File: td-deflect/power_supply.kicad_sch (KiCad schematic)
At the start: 18 parts, among them J1 Conn_01x08_Socket, J1 Conn_01x12_Socket, J18 Conn_01x02_Male, J2 Conn_01x02_Male, J3 Conn_01x04_Male

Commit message: fix drc errors
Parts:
- J18, J2: symbol Connector:Conn_01x02_Male -> Connector:Conn_01x02_Pin
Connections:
- net +3.3V: no longer J1.1 (Pin_1), J1.2 (Pin_2), J3.1 (Pin_1), JP2.2 (B), R30.1
- new net B+C: J1.1 (Pin_1), J1.2 (Pin_2), J3.1 (Pin_1), JP2.2 (B), R30.1

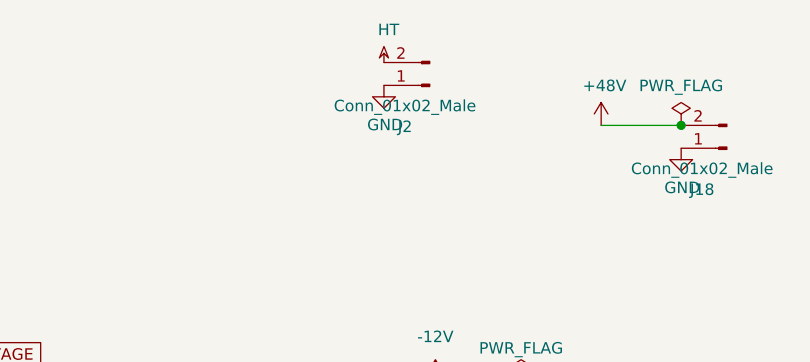
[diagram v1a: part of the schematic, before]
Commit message: fix remaining erc errors
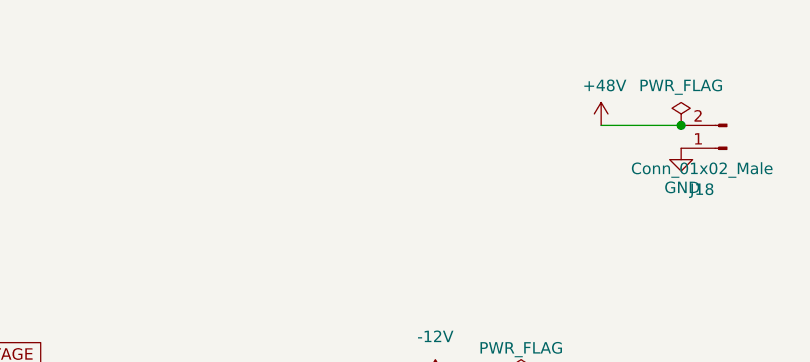
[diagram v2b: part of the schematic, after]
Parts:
- removed J2: Conn_01x02_Male, Connector_Phoenix_MSTB:PhoenixContact_MSTBVA_2,5_2-G_1x02_P5.00mm_Vertical, symbol Connector:Conn_01x02_Pin
- J3: symbol Connector:Conn_01x04_Male -> Connector:Conn_01x04_Pin
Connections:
- net +3.3V renamed B+F
- net B+F: no longer J1.1 (Pin_1), J1.2 (Pin_2), JP1.1 (A), R73.1
- new net B+H: J1.1 (Pin_1), J1.2 (Pin_2), JP1.1 (A), R73.1
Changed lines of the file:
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@@
-    )
-  )
-  (symbol (lib_id "Connector:Conn_01x02_Pin") (at 170.18 24.13 180) (unit 1)
-    (in_bom yes) (on_board yes) (dnp no)
-    (property "Reference" "J2" (at 167.4368 28.7274 0)
-      (effects (font (size 1.27 1.27)))
-    )
-    (property "Value" "Conn_01x02_Male" (at 167.4368 26.416 0)
-      (effects (font (size 1.27 1.27)))
-    )
-    (property "Footprint" "Connector_Phoenix_MSTB:PhoenixContact_MSTBVA_2,5_2-G_1x02_P5.00mm_Vertical" (at 170.18 24.13 0)
-      (effects (font (size 1.27 1.27)) hide)
-    )
-    (property "Datasheet" "~" (at 170.18 24.13 0)
-      (effects (font (size 1.27 1.27)) hide)
-    )
-    (property "Digikey" "277-1150-ND " (at 170.18 24.13 0)
-      (effects (font (size 1.27 1.27)) hide)
-    )
-    (pin "1")
-    (pin "2")
-    (instances
-      (project "td-deflect"
-        (path "/55a1a5e1-4d11-4c3e-b2b4-b9d50ddc5f9d/00000000-0000-0000-0000-00005d9d9196"
-          (reference "J2") (unit 1)
-        )
-      )
-    )
-  )
-  (symbol (lib_id "power:HT") (at 165.1 21.59 0) (unit 1)
-    (in_bom yes) (on_board yes) (dnp no)
-    (property "Reference" "#PWR0101" (at 165.1 18.542 0)
-      (effects (font (size 1.27 1.27)) hide)
-    )
-    (property "Value" "HT" (at 165.608 17.9578 0)
-      (effects (font (size 1.27 1.27)))
-    )
-    (property "Footprint" "" (at 165.1 21.59 0)
-      (effects (font (size 1.27 1.27)) hide)
-    )
-    (property "Datasheet" "" (at 165.1 21.59 0)
-      (effects (font (size 1.27 1.27)) hide)
-    )
-    (pin "1")
-    (instances
-      (project "td-deflect"
-        (path "/55a1a5e1-4d11-4c3e-b2b4-b9d50ddc5f9d/00000000-0000-0000-0000-00005d9d9196"
-          (reference "#PWR0101") (unit 1)
-        )
-      )
-    )
-  )
-  (symbol (lib_id "power:GND") (at 165.1 24.13 0) (unit 1)
-    (in_bom yes) (on_board yes) (dnp no)
-    (property "Reference" "#PWR0102" (at 165.1 30.48 0)
-      (effects (font (size 1.27 1.27)) hide)
-    )
-    (property "Value" "GND" (at 165.227 28.5242 0)
-      (effects (font (size 1.27 1.27)))
-    )
-    (property "Footprint" "" (at 165.1 24.13 0)
-      (effects (font (size 1.27 1.27)) hide)
-    )
-    (property "Datasheet" "" (at 165.1 24.13 0)
-      (effects (font (size 1.27 1.27)) hide)
-    )
-    (pin "1")
-    (instances
-      (project "td-deflect"
-        (path "/55a1a5e1-4d11-4c3e-b2b4-b9d50ddc5f9d/00000000-0000-0000-0000-00005d9d9196"
-          (reference "#PWR0102") (unit 1)
-        )
-      )
     )
   )
@@
     )
   )
-  (symbol (lib_name "PWR_FLAG_1") (lib_id "power:PWR_FLAG") (at 38.1 43.18 0) (unit 1)
+  (symbol (lib_id "power:PWR_FLAG") (at 38.1 43.18 0) (unit 1)
     (in_bom yes) (on_board yes) (dnp no) (fields_autoplaced)
     (property "Reference" "#FLG02" (at 38.1 41.275 0)
@@
     )
   )
-  (symbol (lib_name "PWR_FLAG_1") (lib_id "power:PWR_FLAG") (at 104.14 43.18 0) (unit 1)
+  (symbol (lib_id "power:PWR_FLAG") (at 104.14 43.18 0) (unit 1)
     (in_bom yes) (on_board yes) (dnp no) (fields_autoplaced)
     (property "Reference" "#FLG04" (at 104.14 41.275 0)
@@
     )
   )
-  (symbol (lib_id "Connector:Conn_01x04_Male") (at 259.08 101.6 0) (mirror y) (unit 1)
+  (symbol (lib_id "Connector:Conn_01x04_Pin") (at 259.08 101.6 0) (mirror y) (unit 1)
     (in_bom yes) (on_board yes) (dnp no) (fields_autoplaced)
     (property "Reference" "J3" (at 260.35 101.5999 0)
@@
     )
   )
-  (symbol (lib_name "PWR_FLAG_2") (lib_id "power:PWR_FLAG") (at 173.99 67.31 180) (unit 1)
+  (symbol (lib_id "power:PWR_FLAG") (at 173.99 67.31 180) (unit 1)
     (in_bom yes) (on_board yes) (dnp no) (fields_autoplaced)
     (property "Reference" "#FLG05" (at 173.99 69.215 0)
@@
     )
   )
-  (symbol (lib_name "PWR_FLAG_2") (lib_id "power:PWR_FLAG") (at 180.34 57.15 0) (unit 1)
+  (symbol (lib_id "power:PWR_FLAG") (at 180.34 57.15 0) (unit 1)
     (in_bom yes) (on_board yes) (dnp no) (fields_autoplaced)
     (property "Reference" "#FLG06" (at 180.34 55.245 0)
@@
     )
   )
-  (symbol (lib_name "PWR_FLAG_3") (lib_id "power:PWR_FLAG") (at 212.09 68.58 180) (unit 1)
+  (symbol (lib_id "power:PWR_FLAG") (at 212.09 68.58 180) (unit 1)
     (in_bom yes) (on_board yes) (dnp no) (fields_autoplaced)
     (property "Reference" "#FLG07" (at 212.09 70.485 0)
@@
     )
   )
-  (symbol (lib_name "PWR_FLAG_1") (lib_id "power:PWR_FLAG") (at 71.12 43.18 0) (unit 1)
+  (symbol (lib_id "power:PWR_FLAG") (at 71.12 43.18 0) (unit 1)
     (in_bom yes) (on_board yes) (dnp no) (fields_autoplaced)
     (property "Reference" "#FLG03" (at 71.12 41.275 0)

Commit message: usb
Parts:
- added J17: Barrel_Jack, Connector_BarrelJack:BarrelJack_CLIFF_FC681465S_SMT_Horizontal, symbol Connector:Barrel_Jack_Switch
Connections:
- net +48V: now also J17.1
- net GND: now also J17.2
- no-connect marks 6 -> 7
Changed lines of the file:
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@@
   (junction (at 240.03 104.14) (diameter 0) (color 0 0 0 0)
   )
+  (junction (at 177.8 34.29) (diameter 0) (color 0 0 0 0)
+  )
   (junction (at 167.64 57.15) (diameter 0) (color 0 0 0 0)
   )
@@
   )
   (junction (at 30.48 43.18) (diameter 0) (color 0 0 0 0)
+  )
+  (junction (at 189.23 28.575) (diameter 0) (color 0 0 0 0)
   )
   (junction (at 41.91 43.18) (diameter 0) (color 0 0 0 0)
@@
   (no_connect (at 30.48 38.1))
   (no_connect (at 254 101.6))
+  (no_connect (at 177.8 31.75))
   (no_connect (at 63.5 38.1))
   (no_connect (at 205.74 60.96))
@@
     (stroke (width 0) (type default))
   )
+  (wire (pts (xy 182.88 31.115) (xy 182.88 34.29))
+    (stroke (width 0) (type default))
+  )
   (wire (pts (xy 78.105 33.02) (xy 63.5 33.02))
     (stroke (width 0) (type default))
@@
     (stroke (width 0) (type default))
   )
+  (wire (pts (xy 189.23 28.575) (xy 177.8 28.575))
+    (stroke (width 0) (type default))
+  )
   (wire (pts (xy 60.96 86.36) (xy 66.04 86.36))
     (stroke (width 0) (type default))
@@
     (stroke (width 0) (type default))
   )
+  (wire (pts (xy 198.12 31.115) (xy 182.88 31.115))
+    (stroke (width 0) (type default))
+  )
   (wire (pts (xy 205.74 83.82) (xy 205.74 86.36))
     (stroke (width 0) (type default))
@@
     (stroke (width 0) (type default))
   )
+  (wire (pts (xy 177.8 28.575) (xy 177.8 29.21))
+    (stroke (width 0) (type default))
+  )
   (wire (pts (xy 30.48 43.18) (xy 38.1 43.18))
     (stroke (width 0) (type default))
   )
   (wire (pts (xy 45.085 33.02) (xy 30.48 33.02))
+    (stroke (width 0) (type default))
+  )
+  (wire (pts (xy 182.88 34.29) (xy 177.8 34.29))
     (stroke (width 0) (type default))
   )
@@
         (path "/55a1a5e1-4d11-4c3e-b2b4-b9d50ddc5f9d/00000000-0000-0000-0000-00005d9d9196"
           (reference "J18") (unit 1)
-        )
-      )
-    )
-  )
-  (symbol (lib_id "power:GND") (at 198.12 31.115 0) (unit 1)
-    (in_bom yes) (on_board yes) (dnp no)
-    (property "Reference" "#PWR0119" (at 198.12 37.465 0)
-      (effects (font (size 1.27 1.27)) hide)
-    )
-    (property "Value" "GND" (at 198.247 35.5092 0)
-      (effects (font (size 1.27 1.27)))
-    )
-    (property "Footprint" "" (at 198.12 31.115 0)
-      (effects (font (size 1.27 1.27)) hide)
-    )
-    (property "Datasheet" "" (at 198.12 31.115 0)
-      (effects (font (size 1.27 1.27)) hide)
-    )
-    (pin "1")
-    (instances
-      (project "td-deflect"
-        (path "/55a1a5e1-4d11-4c3e-b2b4-b9d50ddc5f9d/00000000-0000-0000-0000-00005d9d9196"
-          (reference "#PWR0119") (unit 1)
         )
       )
@@
         (path "/55a1a5e1-4d11-4c3e-b2b4-b9d50ddc5f9d/00000000-0000-0000-0000-00005d9d9196"
           (reference "#PWR085") (unit 1)
+        )
+      )
+    )
+  )
+  (symbol (lib_id "power:GND") (at 177.8 34.29 0) (unit 1)
+    (in_bom yes) (on_board yes) (dnp no)
+    (property "Reference" "#PWR036" (at 177.8 40.64 0)
+      (effects (font (size 1.27 1.27)) hide)
+    )
+    (property "Value" "GND" (at 177.927 38.6842 0)
+      (effects (font (size 1.27 1.27)))
+    )
+    (property "Footprint" "" (at 177.8 34.29 0)
+      (effects (font (size 1.27 1.27)) hide)
+    )
+    (property "Datasheet" "" (at 177.8 34.29 0)
+      (effects (font (size 1.27 1.27)) hide)
+    )
+    (pin "1")
+    (instances
+      (project "td-deflect"
+        (path "/55a1a5e1-4d11-4c3e-b2b4-b9d50ddc5f9d/00000000-0000-0000-0000-00005d9d9196"
+          (reference "#PWR036") (unit 1)
         )
       )
@@
         )
       )
+    )
+  )
+  (symbol (lib_id "Connector:Barrel_Jack_Switch") (at 170.18 31.75 0) (unit 1)
+    (in_bom yes) (on_board yes) (dnp no) (fields_autoplaced)
+    (property "Reference" "J17" (at 170.18 24.13 0)
+      (effects (font (size 1.27 1.27)))
+    )
+    (property "Value" "Barrel_Jack" (at 170.18 26.67 0)
+      (effects (font (size 1.27 1.27)))
+    )
+    (property "Footprint" "Connector_BarrelJack:BarrelJack_CLIFF_FC681465S_SMT_Horizontal" (at 171.45 32.766 0)
+      (effects (font (size 1.27 1.27)) hide)
+    )
+    (property "Datasheet" "~" (at 171.45 32.766 0)
+      (effects (font (size 1.27 1.27)) hide)
+    )
+    (pin "1")
+    (pin "2")
+    (pin "3")
+    (instances
+      (project "td-deflect"
+        (path "/55a1a5e1-4d11-4c3e-b2b4-b9d50ddc5f9d/00000000-0000-0000-0000-00005d9d9196"
+          (reference "J17") (unit 1)
+        )
+      )

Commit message: more layout work
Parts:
- added H10, H11, H12, H13, H14, H5, H6, H7, H8, H9: MountingHole, MountingHole:MountingHole_3.2mm_M3, symbol Mechanical:MountingHole
- J1: footprint Connector_PinHeader_2.54mm:PinHeader_1x08_P2.54mm_Horizontal -> Connector_PinSocket_2.54mm:PinSocket_1x08_P2.54mm_Vertical
- J1: footprint Connector_PinHeader_2.54mm:PinHeader_1x12_P2.54mm_Horizontal -> Connector_PinSocket_2.54mm:PinSocket_1x12_P2.54mm_Vertical

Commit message: update pcb
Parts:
- D17: value D_Zener -> 6.3V; footprint Diode_SMD:D_0805_2012Metric_Pad1.15x1.40mm_HandSolder -> Diode_SMD:D_SMA; Digikey (none) -> SMAJ6.5A-FDICT-ND
- F3: Digikey (none) -> 486-3436-ND
- H10, H11, H12, H13, H14, H5, H6, H7, H8, H9, JP1, JP2: Digikey (none) -> DNP
- J1: Digikey (none) -> S7041-ND
- J1: Digikey 609-3323-ND -> S7045-ND
- J17: footprint Connector_BarrelJack:BarrelJack_CLIFF_FC681465S_SMT_Horizontal -> Connector_BarrelJack:BarrelJack_Wuerth_6941xx301002; Digikey (none) -> 732-5930-ND
- J3: Digikey (none) -> 455-B4B-XH-A-ND
- R29, R31, R74: Digikey (none) -> 311-1.00KCRCT-ND
- R30, R6, R73: Digikey (none) -> 311-220KCRCT-ND
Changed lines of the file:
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@@
+      (effects (font (size 1.27 1.27)) hide)
+    )
+    (property "Digikey" "DNP" (at 62.23 15.875 0)
       (effects (font (size 1.27 1.27)) hide)
     )
@@
     )
     (property "Datasheet" "~" (at 74.93 46.99 0)
+      (effects (font (size 1.27 1.27)) hide)
+    )
+    (property "Digikey" " 311-220KCRCT-ND" (at 74.93 46.99 0)
       (effects (font (size 1.27 1.27)) hide)
     )
@@
       (effects (font (size 1.27 1.27)) hide)
     )
+    (property "Digikey" "DNP" (at 203.2 46.355 0)
+      (effects (font (size 1.27 1.27)) hide)
+    )
     (instances
       (project "td-deflect"
@@
       (effects (font (size 1.27 1.27)) hide)
     )
+    (property "Digikey" "DNP" (at 64.77 65.405 0)
+      (effects (font (size 1.27 1.27)) hide)
+    )
     (instances
       (project "td-deflect"
@@
     )
     (property "Datasheet" "~" (at 25.4 35.56 0)
+      (effects (font (size 1.27 1.27)) hide)
+    )
+    (property "Digikey" "S7041-ND" (at 25.4 35.56 0)
       (effects (font (size 1.27 1.27)) hide)
     )
@@
       (effects (font (size 1.27 1.27)) hide)
     )
+    (property "Digikey" " 311-220KCRCT-ND" (at 107.95 46.99 0)
+      (effects (font (size 1.27 1.27)) hide)
+    )
     (pin "1")
     (pin "2")
@@
     )
     (property "Datasheet" "~" (at 167.64 45.72 0)
+      (effects (font (size 1.27 1.27)) hide)
+    )
+    (property "Digikey" "DNP" (at 167.64 45.72 0)
       (effects (font (size 1.27 1.27)) hide)
     )
@@
       (effects (font (size 1.27 1.27)) hide)
     )
+    (property "Digikey" "455-B4B-XH-A-ND" (at 259.08 101.6 0)
+      (effects (font (size 1.27 1.27)) hide)
+    )
     (pin "1")
     (pin "2")
@@
     )
     (property "Datasheet" "~" (at 95.885 16.51 0)
+      (effects (font (size 1.27 1.27)) hide)
+    )
+    (property "Digikey" "DNP" (at 95.885 16.51 0)
       (effects (font (size 1.27 1.27)) hide)
     )
@@
       (effects (font (size 1.27 1.27)) hide)
     )
+    (property "Digikey" "DNP" (at 205.74 95.885 0)
+      (effects (font (size 1.27 1.27)) hide)
+    )
     (instances
       (project "td-deflect"
@@
     )
     (property "Datasheet" "~" (at 58.42 35.56 0)
+      (effects (font (size 1.27 1.27)) hide)
+    )
+    (property "Digikey" "S7041-ND" (at 58.42 35.56 0)
       (effects (font (size 1.27 1.27)) hide)
     )
@@
       (effects (font (size 1.27 1.27)) hide)
     )
+    (property "Digikey" "DNP" (at 26.67 62.865 0)
+      (effects (font (size 1.27 1.27)) hide)
+    )
     (instances
       (project "td-deflect"
@@
       (effects (font (size 1.27 1.27)) hide)
     )
+    (property "Digikey" "DNP" (at 55.88 86.36 0)
+      (effects (font (size 1.27 1.27)) hide)
+    )
     (pin "1")
     (pin "2")
@@
     )
     (property "Datasheet" "~" (at 41.91 62.23 0)
+      (effects (font (size 1.27 1.27)) hide)
+    )
+    (property "Digikey" " 311-1.00KCRCT-ND" (at 41.91 62.23 0)
       (effects (font (size 1.27 1.27)) hide)
     )
@@
       (effects (font (size 1.27 1.27)) hide)
     )
+    (property "Digikey" " 311-1.00KCRCT-ND" (at 74.93 62.23 0)
+      (effects (font (size 1.27 1.27)) hide)
+    )
     (pin "1")
     (pin "2")
@@
     )
     (property "Datasheet" "~" (at 74.93 86.36 0)
+      (effects (font (size 1.27 1.27)) hide)
+    )
+    (property "Digikey" "DNP" (at 74.93 86.36 0)
       (effects (font (size 1.27 1.27)) hide)
     )
@@
       (effects (font (size 1.27 1.27)) hide)
     )
+    (property "Digikey" "DNP" (at 95.885 64.135 0)
+      (effects (font (size 1.27 1.27)) hide)
+    )
     (instances
       (project "td-deflect"
@@
       (effects (font (size 1.27 1.27)) hide)
     )
-    (property "Digikey" "609-3323-ND" (at 162.56 69.85 0)
+    (property "Digikey" "S7045-ND" (at 162.56 69.85 0)
       (effects (font (size 1.27 1.27)) hide)
     )
@@
       (effects (font (size 1.27 1.27)) hide)
     )
-    (property "Digikey" "609-3323-ND" (at 200.66 71.12 0)
+    (property "Digikey" "S7045-ND" (at 200.66 71.12 0)
       (effects (font (size 1.27 1.27)) hide)
     )
@@
       (effects (font (size 1.27 1.27)) hide)
     )
+    (property "Digikey" "DNP" (at 26.67 15.24 0)
+      (effects (font (size 1.27 1.27)) hide)
+    )
     (instances
       (project "td-deflect"
@@
     )
     (property "Datasheet" "~" (at 41.91 46.99 0)
+      (effects (font (size 1.27 1.27)) hide)
+    )
+    (property "Digikey" " 311-220KCRCT-ND" (at 41.91 46.99 0)
       (effects (font (size 1.27 1.27)) hide)
     )
@@
       (effects (font (size 1.27 1.27)) hide)
     )
+    (property "Digikey" " 311-1.00KCRCT-ND" (at 107.95 62.23 0)
+      (effects (font (size 1.27 1.27)) hide)
+    )
     (pin "1")
     (pin "2")
@@
       (effects (font (size 1.27 1.27)) (justify left))
     )
-    (property "Value" "D_Zener" (at 242.57 109.2199 90)
-      (effects (font (size 1.27 1.27)) (justify left))
-    )
-    (property "Footprint" "Diode_SMD:D_0805_2012Metric_Pad1.15x1.40mm_HandSolder" (at 240.03 107.95 0)
+    (property "Value" "6.3V" (at 242.57 109.2199 90)
+      (effects (font (size 1.27 1.27)) (justify left))
+    )
+    (property "Footprint" "Diode_SMD:D_SMA" (at 240.03 107.95 0)
       (effects (font (size 1.27 1.27)) hide)
     )
@@
       (effects (font (size 1.27 1.27)) hide)
     )
+    (property "Digikey" "SMAJ6.5A-FDICT-ND" (at 240.03 107.95 0)
+      (effects (font (size 1.27 1.27)) hide)
+    )
     (pin "1")
     (pin "2")
@@
     )
     (property "Datasheet" "~" (at 167.64 93.345 0)
+      (effects (font (size 1.27 1.27)) hide)
+    )
+    (property "Digikey" "DNP" (at 167.64 93.345 0)
       (effects (font (size 1.27 1.27)) hide)
     )
@@
     )
     (property "Datasheet" "~" (at 91.44 35.56 0)
+      (effects (font (size 1.27 1.27)) hide)
+    )
+    (property "Digikey" "S7041-ND" (at 91.44 35.56 0)
       (effects (font (size 1.27 1.27)) hide)
     )
@@
       (effects (font (size 1.27 1.27)) hide)
     )
+    (property "Digikey" "486-3436-ND" (at 236.22 104.14 0)
+      (effects (font (size 1.27 1.27)) hide)
+    )
     (pin "1")
     (pin "2")
@@
       (effects (font (size 1.27 1.27)))
     )
-    (property "Footprint" "Connector_BarrelJack:BarrelJack_CLIFF_FC681465S_SMT_Horizontal" (at 171.45 32.766 0)
+    (property "Footprint" "Connector_BarrelJack:BarrelJack_Wuerth_6941xx301002" (at 171.45 32.766 0)
       (effects (font (size 1.27 1.27)) hide)
     )
@@
       (effects (font (size 1.27 1.27)) hide)
     )
+    (property "Digikey" "732-5930-ND" (at 170.18 31.75 0)
+      (effects (font (size 1.27 1.27)) hide)
+    )
